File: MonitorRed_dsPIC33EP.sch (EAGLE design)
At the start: 20 parts, among them IC1 LP2950CDT-3.0, IC2 DSPIC33FJ12GP202/SP, X1 22-23-2021, X2 22-23-2021, X3 22-23-2021

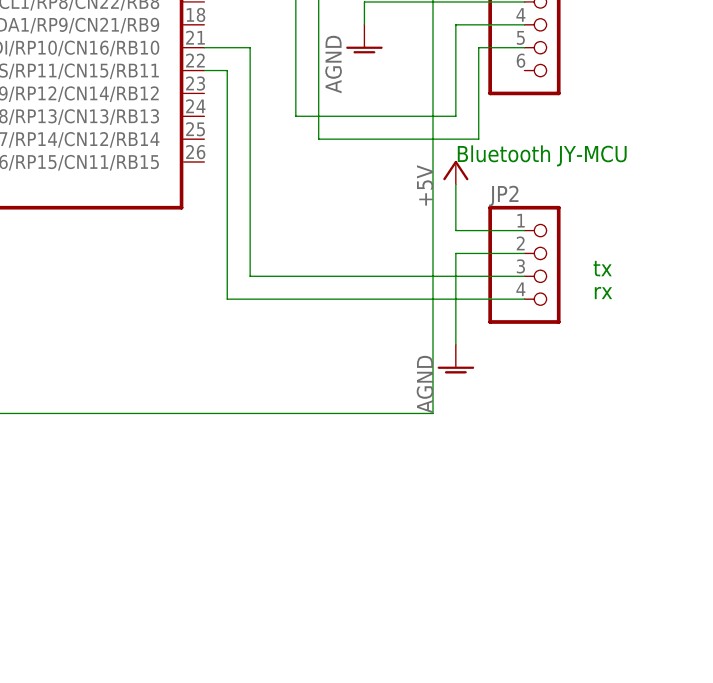
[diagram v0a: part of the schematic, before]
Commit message: añade ds18b20 en esquema
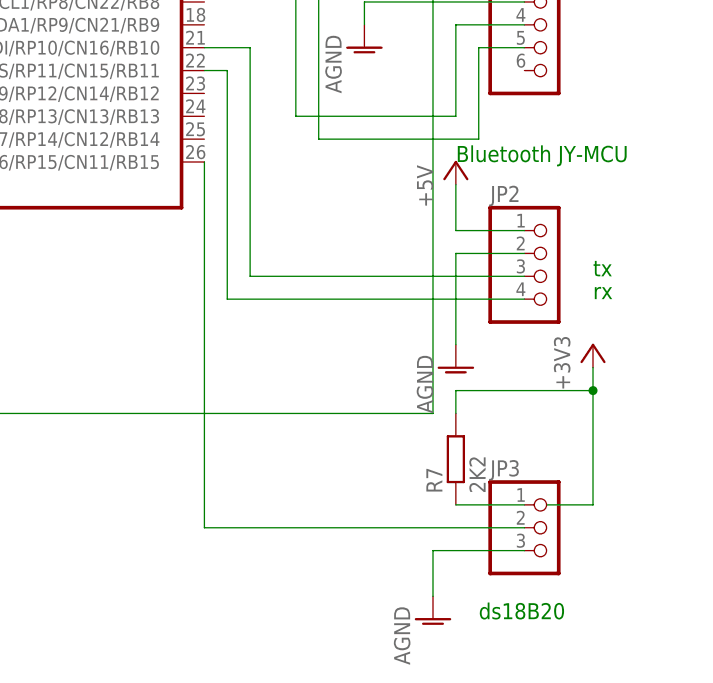
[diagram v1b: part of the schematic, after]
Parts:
- added JP3: (no value), pinhead:PINHD-1X3
- added R7: 2K2, rcl:R-EU_M0805
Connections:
- new net N$15: IC2.AN6/RP15/CN11/RB15, JP3.2
- new net N$16: JP3.1, R7.1
- net +3V3: now also R7.2
- net AGND: now also JP3.3
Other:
- note added: "ds18B20"
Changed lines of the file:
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@@
 <part name="P+1" library="supply1" deviceset="+5V" device=""/>
 <part name="P+2" library="supply1" deviceset="+5V" device=""/>
+<part name="JP3" library="pinhead" deviceset="PINHD-1X3" device=""/>
+<part name="&quot;&quot;9" library="supply1" deviceset="AGND" device=""/>
+<part name="R7" library="rcl" deviceset="R-EU_" device="M0805" value="2K2"/>
+<part name="+3V7" library="supply1" deviceset="+3V3" device=""/>
 </parts>
 <sheets>
@@
 <text x="162.56" y="132.08" size="1.778" layer="91">tx</text>
 <text x="162.56" y="129.54" size="1.778" layer="91">rx</text>
+<text x="149.86" y="93.98" size="1.778" layer="91">ds18B20</text>
 </plain>
 <instances>
@@
 <instance part="P+1" gate="1" x="27.94" y="259.08"/>
 <instance part="P+2" gate="1" x="147.32" y="144.78"/>
+<instance part="JP3" gate="A" x="157.48" y="104.14"/>
+<instance part="&quot;&quot;9" gate="VR1" x="144.78" y="93.98"/>
+<instance part="R7" gate="G$1" x="147.32" y="111.76" rot="R90"/>
+<instance part="+3V7" gate="G$1" x="162.56" y="124.46"/>
 </instances>
 <busses>
@@
 <pinref part="&quot;&quot;8" gate="VR1" pin="AGND"/>
 <wire x1="147.32" y1="134.62" x2="147.32" y2="124.46" width="0.1524" layer="91"/>
+</segment>
+<segment>
+<pinref part="JP3" gate="A" pin="3"/>
+<wire x1="154.94" y1="101.6" x2="144.78" y2="101.6" width="0.1524" layer="91"/>
+<pinref part="&quot;&quot;9" gate="VR1" pin="AGND"/>
+<wire x1="144.78" y1="101.6" x2="144.78" y2="96.52" width="0.1524" layer="91"/>
 </segment>
 </net>
@@
 <pinref part="+3V6" gate="G$1" pin="+3V3"/>
 <wire x1="0" y1="149.86" x2="0" y2="152.4" width="0.1524" layer="91"/>
+</segment>
+<segment>
+<pinref part="+3V7" gate="G$1" pin="+3V3"/>
+<wire x1="157.48" y1="106.68" x2="162.56" y2="106.68" width="0.1524" layer="91"/>
+<wire x1="162.56" y1="106.68" x2="162.56" y2="119.38" width="0.1524" layer="91"/>
+<pinref part="R7" gate="G$1" pin="2"/>
+<wire x1="162.56" y1="119.38" x2="162.56" y2="121.92" width="0.1524" layer="91"/>
+<wire x1="147.32" y1="119.38" x2="147.32" y2="116.84" width="0.1524" layer="91"/>
+<wire x1="147.32" y1="119.38" x2="162.56" y2="119.38" width="0.1524" layer="91"/>
+<junction x="162.56" y="119.38"/>
 </segment>
 </net>
@@
 </segment>
 </net>
+<net name="N$15" class="0">
+<segment>
+<pinref part="JP3" gate="A" pin="2"/>
+<pinref part="IC2" gate="X" pin="AN6/RP15/CN11/RB15"/>
+<wire x1="154.94" y1="104.14" x2="119.38" y2="104.14" width="0.1524" layer="91"/>
+<wire x1="119.38" y1="104.14" x2="119.38" y2="144.78" width="0.1524" layer="91"/>
+</segment>
+</net>
+<net name="N$16" class="0">
+<segment>
+<pinref part="JP3" gate="A" pin="1"/>
+<pinref part="R7" gate="G$1" pin="1"/>
+<wire x1="154.94" y1="106.68" x2="147.32" y2="106.68" width="0.1524" layer="91"/>
+</segment>
+</net>

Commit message: Cambio esquema
cambio esquema
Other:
- moved on the sheet: LED1
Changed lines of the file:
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@@
 <?xml version="1.0" encoding="utf-8"?>
 <!DOCTYPE eagle SYSTEM "eagle.dtd">
-<eagle version="6.3">
+<eagle version="7.1.0">
 <drawing>
 <settings>
@@
 <part name="LED1" library="led" deviceset="LED" device="5MM"/>
 <part name="R5" library="rcl" deviceset="R-EU_" device="M0805" value="330"/>
-<part name="+3V6" library="supply1" deviceset="+3V3" device=""/>
 <part name="JP2" library="pinhead" deviceset="PINHD-1X4" device="/90"/>
 <part name="&quot;&quot;8" library="supply1" deviceset="AGND" device=""/>
@@
 <part name="R7" library="rcl" deviceset="R-EU_" device="M0805" value="2K2"/>
 <part name="+3V7" library="supply1" deviceset="+3V3" device=""/>
+<part name="+3V6" library="supply1" deviceset="+3V3" device=""/>
 </parts>
 <sheets>
@@
 <instance part="R3" gate="G$1" x="15.24" y="210.82" rot="R90"/>
 <instance part="R6" gate="G$1" x="15.24" y="195.58" rot="R90"/>
-<instance part="LED1" gate="G$1" x="0" y="147.32"/>
+<instance part="LED1" gate="G$1" x="0" y="147.32" rot="R90"/>
 <instance part="R5" gate="G$1" x="12.7" y="147.32" rot="R180"/>
-<instance part="+3V6" gate="G$1" x="0" y="154.94"/>
 <instance part="JP2" gate="A" x="157.48" y="132.08"/>
 <instance part="&quot;&quot;8" gate="VR1" x="147.32" y="121.92"/>
@@
 <instance part="R7" gate="G$1" x="147.32" y="111.76" rot="R90"/>
 <instance part="+3V7" gate="G$1" x="162.56" y="124.46"/>
+<instance part="+3V6" gate="G$1" x="-7.62" y="154.94"/>
 </instances>
 <busses>
@@
 </segment>
 <segment>
-<pinref part="LED1" gate="G$1" pin="A"/>
-<pinref part="+3V6" gate="G$1" pin="+3V3"/>
-<wire x1="0" y1="149.86" x2="0" y2="152.4" width="0.1524" layer="91"/>
-</segment>
-<segment>
 <pinref part="+3V7" gate="G$1" pin="+3V3"/>
 <wire x1="157.48" y1="106.68" x2="162.56" y2="106.68" width="0.1524" layer="91"/>
@@
 <wire x1="147.32" y1="119.38" x2="162.56" y2="119.38" width="0.1524" layer="91"/>
 <junction x="162.56" y="119.38"/>
+</segment>
+<segment>
+<pinref part="+3V6" gate="G$1" pin="+3V3"/>
+<wire x1="-7.62" y1="152.4" x2="-7.62" y2="147.32" width="0.1524" layer="91"/>
+<pinref part="LED1" gate="G$1" pin="A"/>
+<wire x1="-7.62" y1="147.32" x2="-2.54" y2="147.32" width="0.1524" layer="91"/>
 </segment>
 </net>
@@
 </segment>
 </net>
-<net name="N$10" class="0">
-<segment>
-<pinref part="LED1" gate="G$1" pin="C"/>
-<wire x1="0" y1="142.24" x2="0" y2="139.7" width="0.1524" layer="91"/>
-<wire x1="0" y1="139.7" x2="7.62" y2="139.7" width="0.1524" layer="91"/>
-<pinref part="R5" gate="G$1" pin="2"/>
-<wire x1="7.62" y1="139.7" x2="7.62" y2="147.32" width="0.1524" layer="91"/>
-</segment>
-</net>
 <net name="+5V" class="0">
 <segment>
@@
 </segment>
 </net>
+<net name="N$1" class="0">
+<segment>
+<pinref part="LED1" gate="G$1" pin="C"/>
+<pinref part="R5" gate="G$1" pin="2"/>
+<wire x1="5.08" y1="147.32" x2="7.62" y2="147.32" width="0.1524" layer="91"/>
+</segment>
+</net>

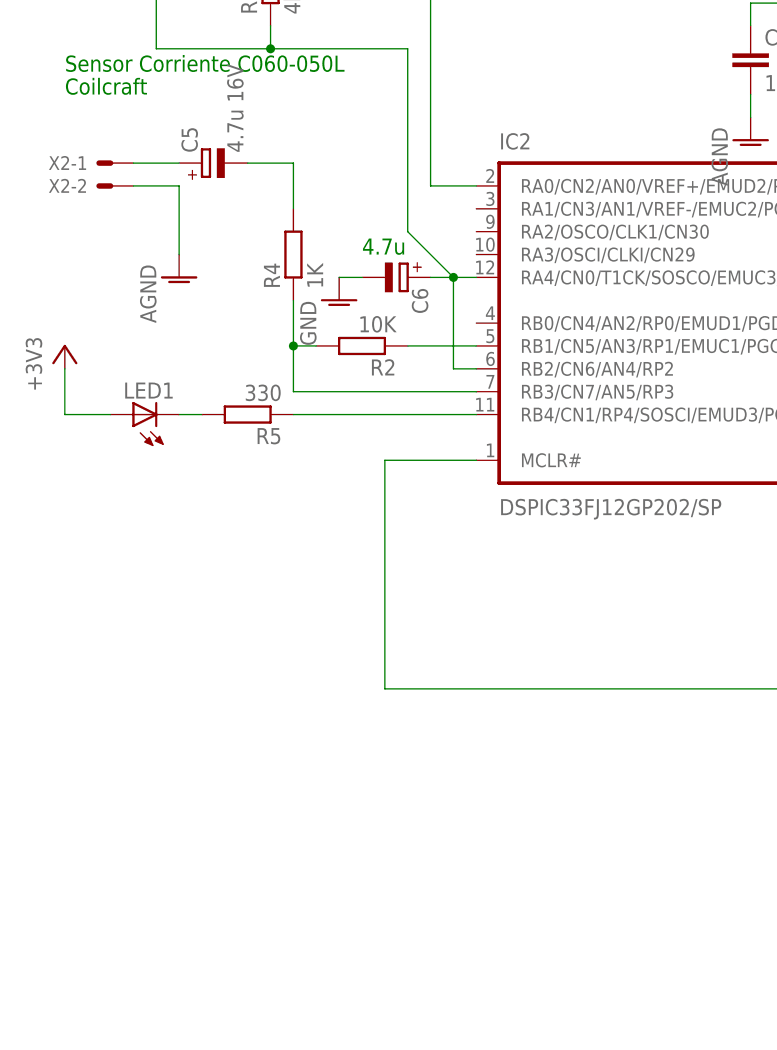
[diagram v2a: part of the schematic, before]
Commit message: se modifica para diodo schoky
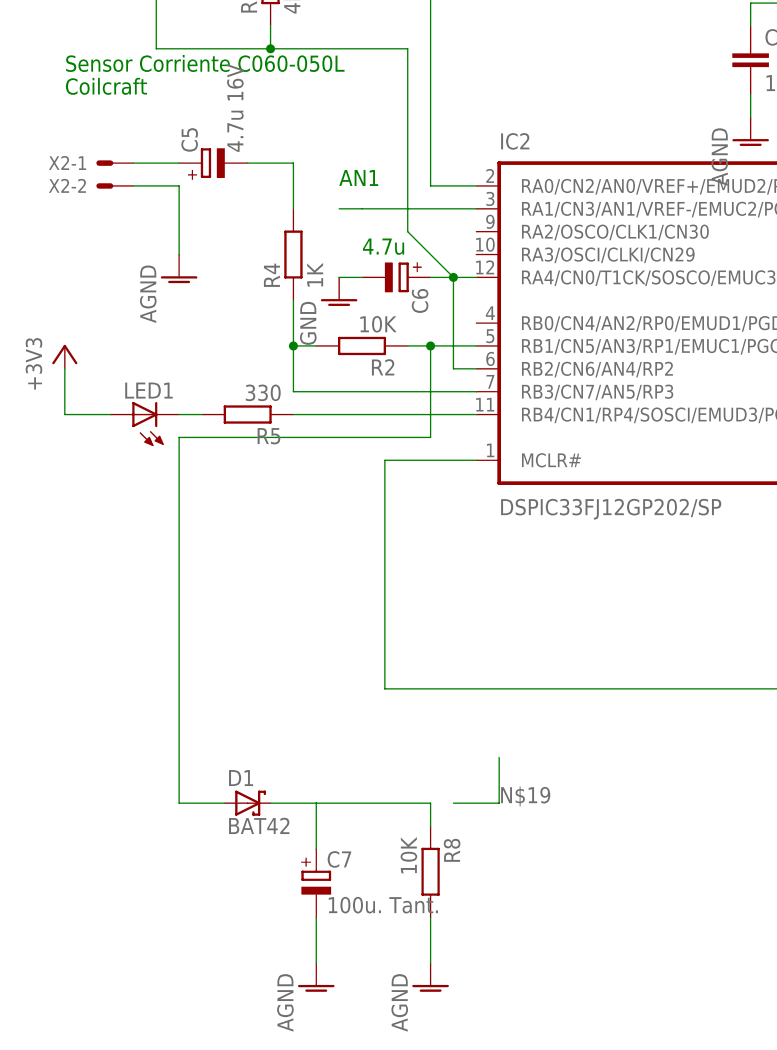
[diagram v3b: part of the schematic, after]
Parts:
- added C7: 100u. Tant., rcl:CPOL-EUA/3216-18R
- added D1: BAT42, diode:BAT42
- added R8: 10K, rcl:R-EU_M0805
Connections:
- new net AN1: C7.+, D1.C, R8.1
- new net N$10: IC2.RA1/CN3/AN1/VREF-/EMUC2/PGC2
- net AGND: now also C7.-, R8.2
- net N$4: now also D1.A
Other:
- note added: "AN1"
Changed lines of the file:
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@@
 <layer number="97" name="Info" color="7" fill="1" visible="yes" active="yes"/>
 <layer number="98" name="Guide" color="6" fill="1" visible="yes" active="yes"/>
+<layer number="99" name="SpiceOrder" color="5" fill="1" visible="yes" active="yes"/>
 </layers>
 <schematic xreflabel="%F%N/%S.%C%R" xrefpart="/%S.%C%R">
@@
 <part name="+3V7" library="supply1" deviceset="+3V3" device=""/>
 <part name="+3V6" library="supply1" deviceset="+3V3" device=""/>
+<part name="D1" library="diode" deviceset="BAT42" device=""/>
+<part name="C7" library="rcl" deviceset="CPOL-EU" device="A/3216-18R" value="100u. Tant."/>
+<part name="R8" library="rcl" deviceset="R-EU_" device="M0805" value="10K"/>
+<part name="&quot;&quot;10" library="supply1" deviceset="AGND" device=""/>
+<part name="&quot;&quot;11" library="supply1" deviceset="AGND" device=""/>
 </parts>
 <sheets>
@@
 <text x="162.56" y="129.54" size="1.778" layer="91">rx</text>
 <text x="149.86" y="93.98" size="1.778" layer="91">ds18B20</text>
+<text x="22.86" y="172.72" size="1.778" layer="91">AN1</text>
 </plain>
 <instances>
@@
 <instance part="+3V7" gate="G$1" x="162.56" y="124.46"/>
 <instance part="+3V6" gate="G$1" x="-7.62" y="154.94"/>
+<instance part="D1" gate="1" x="12.7" y="104.14"/>
+<instance part="C7" gate="G$1" x="20.32" y="96.52"/>
+<instance part="R8" gate="G$1" x="33.02" y="96.52" rot="R270"/>
+<instance part="&quot;&quot;10" gate="VR1" x="20.32" y="83.82"/>
+<instance part="&quot;&quot;11" gate="VR1" x="33.02" y="83.82"/>
 </instances>
 <busses>
@@
 <pinref part="&quot;&quot;9" gate="VR1" pin="AGND"/>
 <wire x1="144.78" y1="101.6" x2="144.78" y2="96.52" width="0.1524" layer="91"/>
+</segment>
+<segment>
+<pinref part="C7" gate="G$1" pin="-"/>
+<pinref part="&quot;&quot;10" gate="VR1" pin="AGND"/>
+<wire x1="20.32" y1="91.44" x2="20.32" y2="86.36" width="0.1524" layer="91"/>
+</segment>
+<segment>
+<pinref part="&quot;&quot;11" gate="VR1" pin="AGND"/>
+<pinref part="R8" gate="G$1" pin="2"/>
+<wire x1="33.02" y1="86.36" x2="33.02" y2="91.44" width="0.1524" layer="91"/>
 </segment>
 </net>
@@
 <pinref part="R2" gate="G$1" pin="1"/>
 <pinref part="IC2" gate="X" pin="RB1/CN5/AN3/RP1/EMUC1/PGC1"/>
-<wire x1="38.1" y1="154.94" x2="30.48" y2="154.94" width="0.1524" layer="91"/>
+<wire x1="38.1" y1="154.94" x2="33.02" y2="154.94" width="0.1524" layer="91"/>
+<junction x="33.02" y="154.94"/>
+<wire x1="33.02" y1="154.94" x2="30.48" y2="154.94" width="0.1524" layer="91"/>
+<wire x1="33.02" y1="154.94" x2="33.02" y2="144.78" width="0.1524" layer="91"/>
+<wire x1="33.02" y1="144.78" x2="5.08" y2="144.78" width="0.1524" layer="91"/>
+<pinref part="D1" gate="1" pin="A"/>
+<wire x1="10.16" y1="104.14" x2="5.08" y2="104.14" width="0.1524" layer="91"/>
+<wire x1="5.08" y1="104.14" x2="5.08" y2="144.78" width="0.1524" layer="91"/>
 </segment>
 </net>
@@
 </segment>
 </net>
+<net name="AN1" class="0">
+<segment>
+<pinref part="D1" gate="1" pin="C"/>
+<wire x1="15.24" y1="104.14" x2="20.32" y2="104.14" width="0.1524" layer="91"/>
+<pinref part="R8" gate="G$1" pin="1"/>
+<wire x1="20.32" y1="104.14" x2="33.02" y2="104.14" width="0.1524" layer="91"/>
+<wire x1="33.02" y1="104.14" x2="33.02" y2="101.6" width="0.1524" layer="91"/>
+<pinref part="C7" gate="G$1" pin="+"/>
+<wire x1="20.32" y1="99.06" x2="20.32" y2="104.14" width="0.1524" layer="91"/>
+</segment>
+</net>
+<net name="N$10" class="0">
+<segment>
+<pinref part="IC2" gate="X" pin="RA1/CN3/AN1/VREF-/EMUC2/PGC2"/>
+<wire x1="38.1" y1="170.18" x2="25.4" y2="170.18" width="0.1524" layer="91"/>
+<wire x1="22.86" y1="170.18" x2="25.4" y2="170.18" width="0.1524" layer="91"/>
+</segment>
+</net>
+<net name="N$19" class="0">
+<segment>
+<wire x1="40.64" y1="104.14" x2="40.64" y2="109.22" width="0.1524" layer="91"/>
+<wire x1="40.64" y1="104.14" x2="35.56" y2="104.14" width="0.1524" layer="91"/>
+<label x="40.64" y="104.14" size="1.778" layer="95"/>
+</segment>
+</net>
